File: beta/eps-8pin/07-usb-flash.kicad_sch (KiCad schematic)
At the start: 7 parts, among them J5 USB-C 2.0

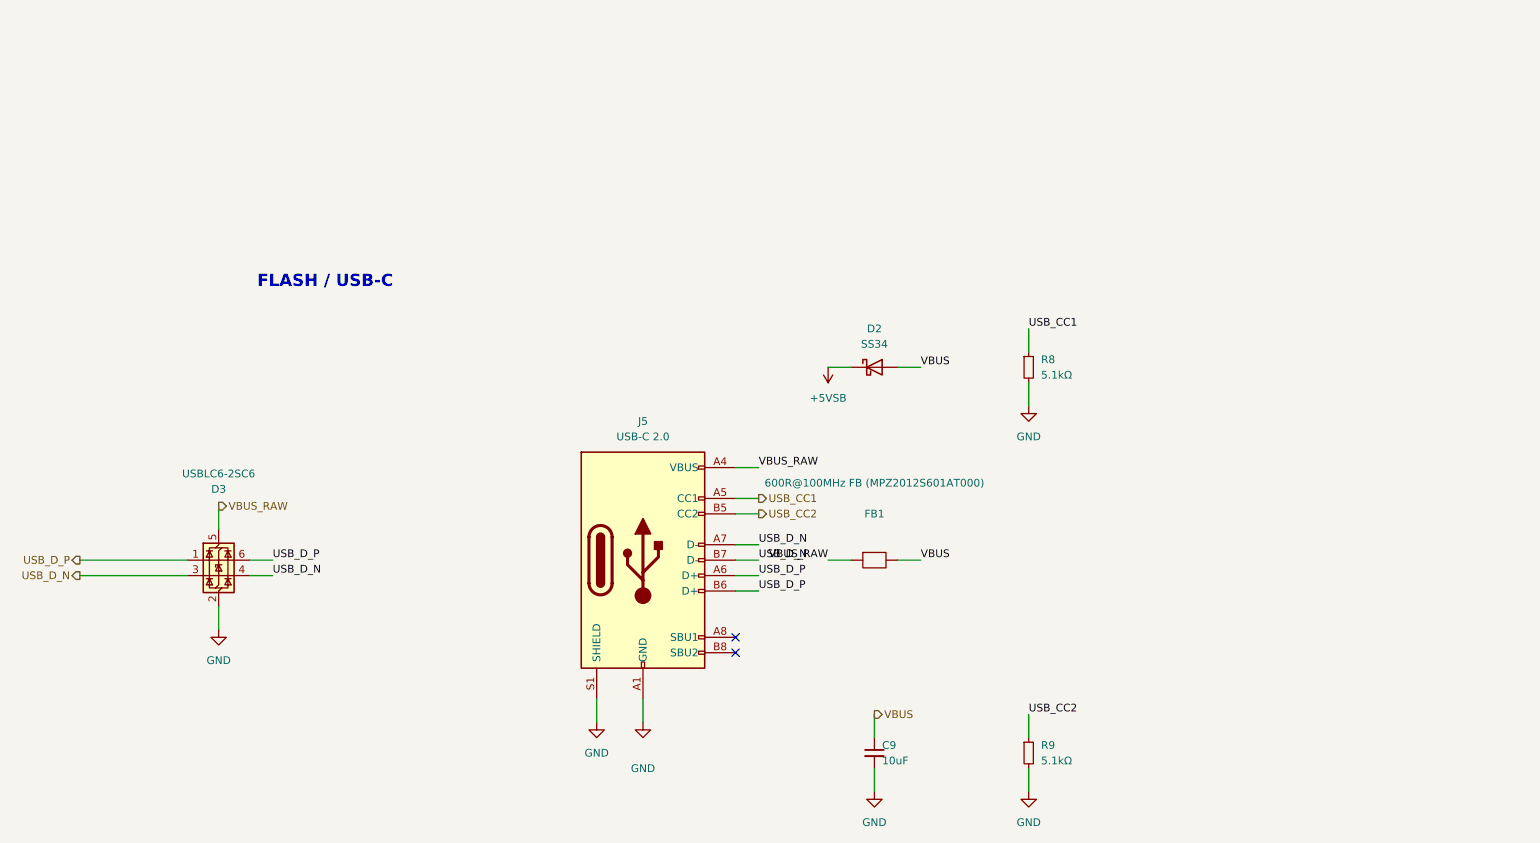
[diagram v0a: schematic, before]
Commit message: eps-8pin: USB-ingress TPS2121 mux replaces the D2 SS34 ORing diode (spec v1.6.0 Sec 6.14)
Owner rulings 2026-07-24 (docs/usb-ingress-bom-delta-2026-07-24.md Sec 3.1): the SS34
ORing diode let host VBUS forward-feed straight into the PSU-side 5VSB bulk through a
dead/faulted PSU (sim-confirmed ~27A peak). Replaces it with U4 = TPS2121RUXR:
IN1 = the RJ-45 VCC feed after the existing FB2 bead (now a cross-sheet net, since it
originates in 01-hub-link.kicad_sch -- carried via a global_label "VCC_RJ45", the
documented cec_sch.py primitive for a net crossing sibling leaf sheets with no direct
sheet-pin lane); IN2 = VBUS behind a new polyfuse F1 inserted ahead of the existing FB1
bead; OUT = +5VSB (the same rail every existing load already sits on). OV1/PR1 get real
dividers off IN1 (R15/R16, R17/R18); CP2/OV2/GND strap to GND; ILIM (R14) and SS (C42)
per the datasheet. D2 removed entirely.

Refdes: the doc's proposed R13/C41 collided with an unrelated existing 10k/100nF pair
added since the doc's 2026-07-24 refdes check -- shifted to R14-R18/C42-C44 (same
internal ordering). U4/F1 were free as proposed.

Deviation, flagged (not silent): ST (pin 9, "Output" type) is left a genuine no_connect
rather than hard-grounded per the doc's literal "CP2, OV2, ST -> GND" -- grounding it
put two ERC-classified drivers ("Output" + PWR_FLAG's "Power output") on one net, a real
pin_to_pin ERROR (not the usual benign-warning class). NC matches the datasheet's own
alternative for an unused pin and the hub's own as-built U5/U7 precedent for this pin.

Vendored a real cec-Resistor_SMD:R_1206_3216Metric footprint + 3D model (F1's 1206
package; none existed in this repo before, only 0402/0805/2512) from the local KiCad 10
install, KIPRJMOD-relativized per the repo's library convention, kicad-cli fp-upgraded.
Added the cec-Package_DFN_QFN library to eps-8pin's fp-lib-table (already used by the
hub/24-pin's own TPS2121 instances, missing here since EPS never had one before).

Gates: ERC 105->11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
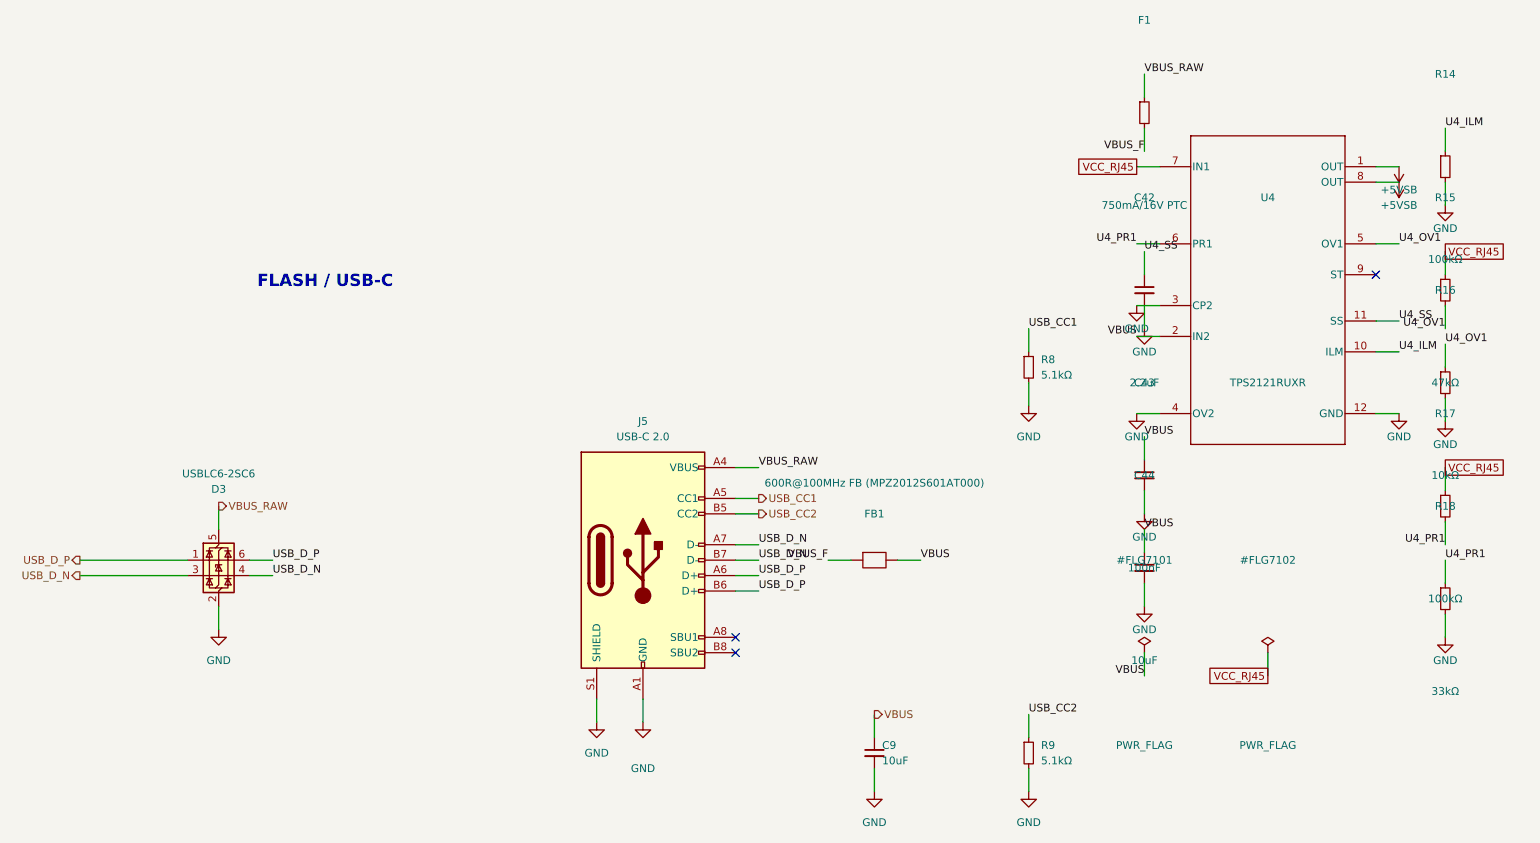
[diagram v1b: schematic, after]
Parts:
- removed D2: SS34, cec-Diode_SMD:D_SMA, symbol cec-vendor:D_Schottky
- added C42: 2.2uF, cec-Capacitor_SMD:C_0603_1608Metric, symbol cec-vendor:C_Small
- added C43: 100nF, cec-Capacitor_SMD:C_0402_1005Metric, symbol cec-vendor:C_Small
- added C44: 10uF, cec-Capacitor_SMD:C_0805_2012Metric, symbol cec-vendor:C_Small
- added F1: 750mA/16V PTC, cec-Resistor_SMD:R_1206_3216Metric, symbol cec-vendor:R_Small
- added R14, R17: 100kΩ, cec-Resistor_SMD:R_0402_1005Metric, symbol cec-vendor:R_Small
- added R15: 47kΩ, cec-Resistor_SMD:R_0402_1005Metric, symbol cec-vendor:R_Small
- added R16: 10kΩ, cec-Resistor_SMD:R_0402_1005Metric, symbol cec-vendor:R_Small
- added R18: 33kΩ, cec-Resistor_SMD:R_0402_1005Metric, symbol cec-vendor:R_Small
- added U4: TPS2121RUXR, cec-Package_DFN_QFN:RUX0012A, symbol cec-vendor:TPS2121RUXR
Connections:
- net +5VSB: now also U4.1 (OUT), U4.8 (OUT)
- net GND: now also C42.2, C43.2, C44.2, R14.2, R16.2, R18.2, U4.12 (GND), U4.3 (CP2), U4.4 (OV2)
- net VBUS: now also C43.1, C44.1, U4.2 (IN2)
- net VBUS_RAW: now also F1.1; no longer FB1.1
- new net U4_ILM: R14.1, U4.10 (ILM)
- new net U4_OV1: R15.2, R16.1, U4.5 (OV1)
- new net U4_PR1: R17.2, R18.1, U4.6 (PR1)
- new net U4_SS: C42.1, U4.11 (SS)
- new net VBUS_F: F1.2, FB1.1
- new net VCC_RJ45: R15.1, R17.1, U4.7 (IN1)
- no-connect marks 2 -> 3
